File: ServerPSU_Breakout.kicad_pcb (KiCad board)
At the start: 2 copper layers, 120 x 90 mm, 25 parts, among them J1 Conn_01x05, J2 Conn_01x14, J3 Conn_01x01, J4 Conn_01x01, Q1 DMG2302U, U1 NCS1S1203SC, U2 STM32F072RBTx

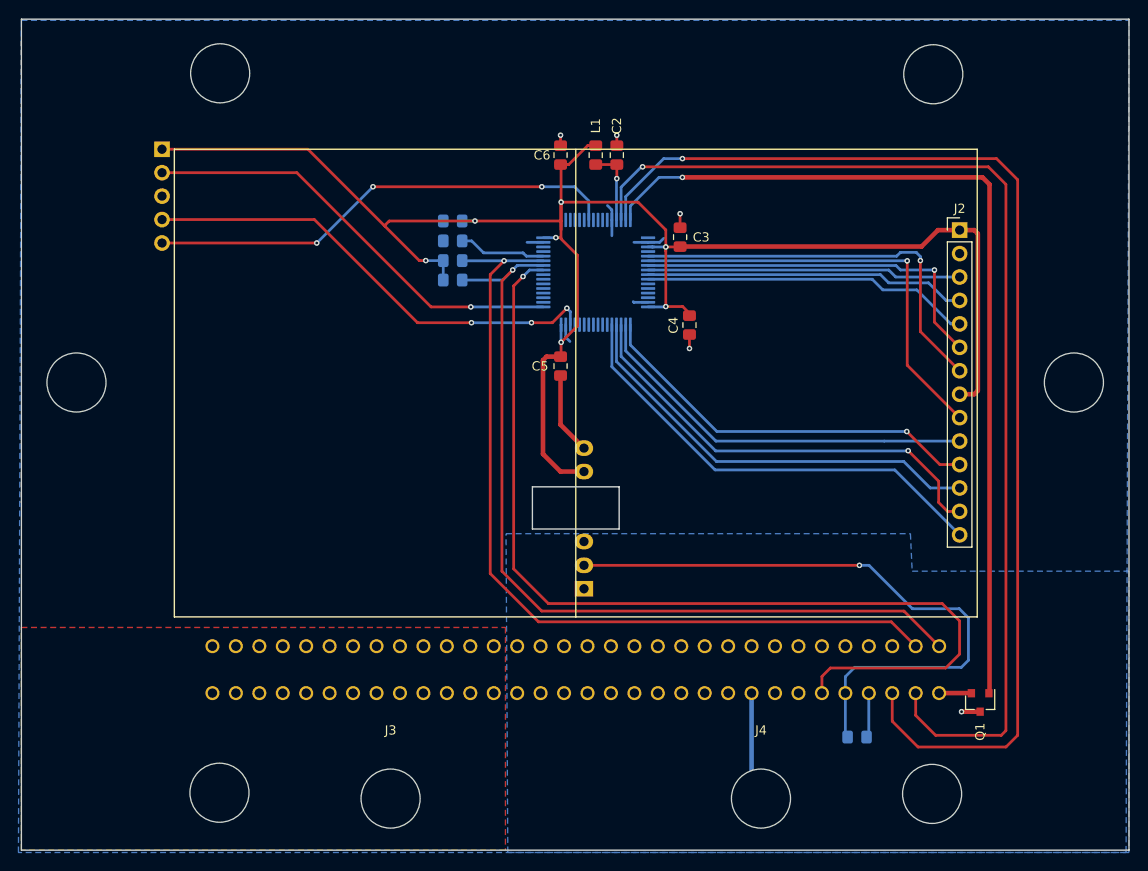
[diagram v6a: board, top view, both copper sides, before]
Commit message: updated hw
- added SMBUS address HW 
- Changed Isolated DC Module to TI SimpleSwitcher IC
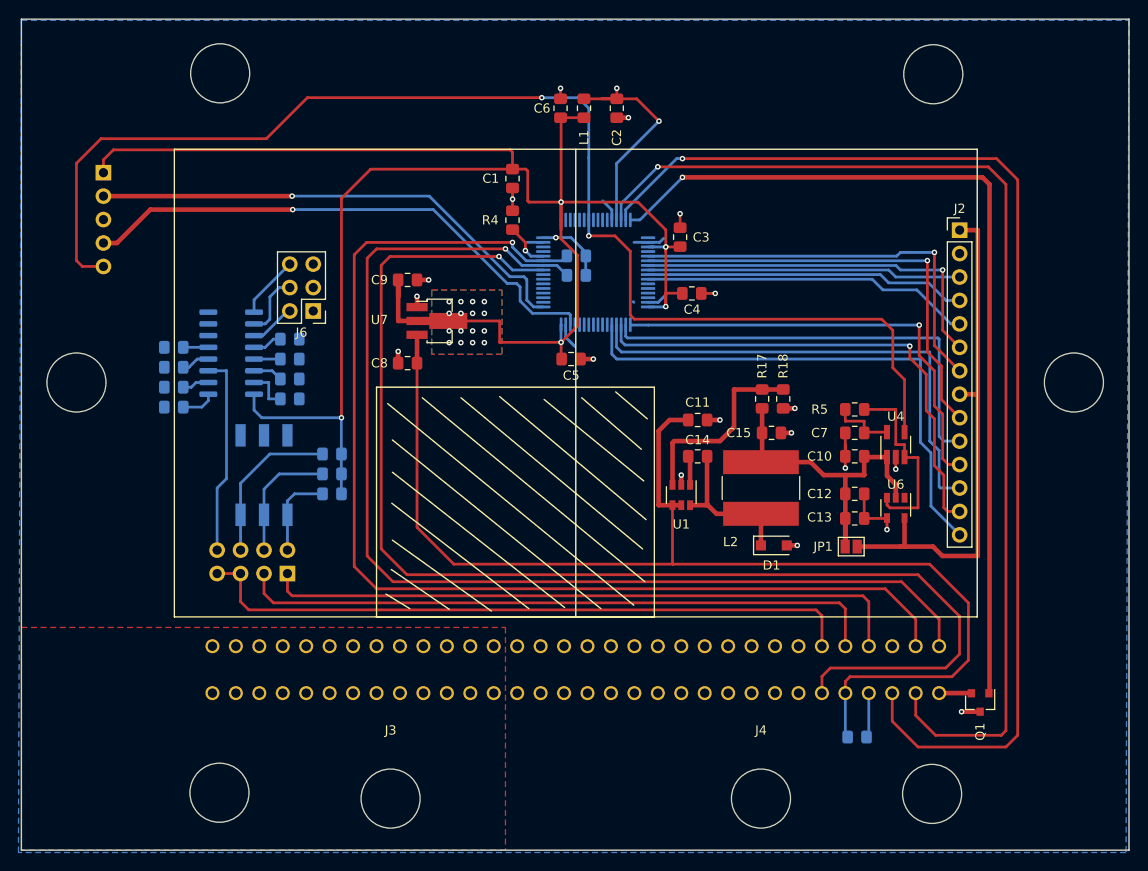
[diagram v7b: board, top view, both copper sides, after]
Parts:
- added C10: 100nF, Capacitor_SMD:C_0805_2012Metric_Pad1.15x1.40mm_HandSolder, F.Cu at (191.9, 94.2)
- added C11: 4.7uF X5R 25V, Capacitor_SMD:C_0805_2012Metric_Pad1.15x1.40mm_HandSolder, F.Cu at (174.9, 90.3)
- added C12: 1uF Low ESR, Capacitor_SMD:C_0805_2012Metric_Pad1.15x1.40mm_HandSolder, F.Cu at (191.9, 98.3)
- added C13: 100nF Low ESR, Capacitor_SMD:C_0805_2012Metric_Pad1.15x1.40mm_HandSolder, F.Cu at (191.9, 101.0)
- added C14: 200nF, Capacitor_SMD:C_0805_2012Metric_Pad1.15x1.40mm_HandSolder, F.Cu at (174.9, 94.2)
- added C15: 33uF X5R 10V, Capacitor_SMD:C_0805_2012Metric_Pad1.15x1.40mm_HandSolder, F.Cu at (182.9, 91.7)
- added C7: 2.2uF, Capacitor_SMD:C_0805_2012Metric_Pad1.15x1.40mm_HandSolder, F.Cu at (191.9, 91.7)
- added C8: 100nF, Capacitor_SMD:C_0805_2012Metric_Pad1.15x1.40mm_HandSolder, F.Cu at (143.4, 84.1)
- added C9: 100nF, Capacitor_SMD:C_0805_2012Metric_Pad1.15x1.40mm_HandSolder, F.Cu at (143.4, 75.1)
- added D1: SS14L, Diode_SMD:D_SOD-123F, F.Cu at (183.1, 103.9)
- added J5: Conn_02x04_Odd_Even, Connector_PinHeader_2.54mm:PinHeader_2x04_P2.54mm_Vertical, B.Cu at (130.4, 106.9)
- added J6: Conn_02x03_Odd_Even, Connector_PinHeader_2.54mm:PinHeader_2x03_P2.54mm_Vertical, F.Cu at (133.2, 78.5)
- added JP1: Jumper_NO_Small, Jumper:SolderJumper-2_P1.3mm_Open_Pad1.0x1.5mm, F.Cu at (191.5, 104.0)
- added L2: 18uH 150mOhm, Inductor_SMD:L_Bourns-SRN8040_8x8.15mm, F.Cu at (181.7, 97.7)
- added R10: 2K2, Resistor_SMD:R_0805_2012Metric_Pad1.15x1.40mm_HandSolder, B.Cu at (130.7, 85.9)
- added R11: 4K6, Resistor_SMD:R_0805_2012Metric_Pad1.15x1.40mm_HandSolder, B.Cu at (130.7, 88.0)
- added R12: 7K5, Resistor_SMD:R_0805_2012Metric_Pad1.15x1.40mm_HandSolder, B.Cu at (130.7, 81.5)
- added R13: 12K7, Resistor_SMD:R_0805_2012Metric_Pad1.15x1.40mm_HandSolder, B.Cu at (118.1, 88.9)
- added R14: 21K5, Resistor_SMD:R_0805_2012Metric_Pad1.15x1.40mm_HandSolder, B.Cu at (118.1, 82.4)
- added R15: 48K7, Resistor_SMD:R_0805_2012Metric_Pad1.15x1.40mm_HandSolder, B.Cu at (118.1, 86.7)
- added R16: 100K, Resistor_SMD:R_0805_2012Metric_Pad1.15x1.40mm_HandSolder, B.Cu at (118.1, 84.6)
- added R17: 5.6K, Resistor_SMD:R_0805_2012Metric_Pad1.15x1.40mm_HandSolder, F.Cu at (181.9, 88.0)
- added R18: 1K, Resistor_SMD:R_0805_2012Metric_Pad1.15x1.40mm_HandSolder, F.Cu at (184.2, 88.0)
- added R5: 1Meg, Resistor_SMD:R_0805_2012Metric_Pad1.15x1.40mm_HandSolder, F.Cu at (191.9, 89.2)
- added R6: 4K7, Resistor_SMD:R_0805_2012Metric_Pad1.15x1.40mm_HandSolder, B.Cu at (135.3, 98.3)
- added R7: 4K7, Resistor_SMD:R_0805_2012Metric_Pad1.15x1.40mm_HandSolder, B.Cu at (135.3, 96.1)
- added R8: 4K7, Resistor_SMD:R_0805_2012Metric_Pad1.15x1.40mm_HandSolder, B.Cu at (135.3, 94.0)
- added R9: 0R, Resistor_SMD:R_0805_2012Metric_Pad1.15x1.40mm_HandSolder, B.Cu at (130.7, 83.7)
- added SW1: SW_DIP_x03, Button_Switch_SMD:SW_DIP_SPSTx03_Slide_6.7x9.18mm_W8.61mm_P2.54mm_LowProfile, B.Cu at (127.9, 96.3)
- added U3: 4051, Package_SO:SOIC-16_3.9x9.9mm_P1.27mm, B.Cu at (124.3, 83.1)
- added U4: MIC1555-YM5, Package_TO_SOT_SMD:SOT-23-5_HandSoldering, F.Cu at (196.3, 93.0)
- added U6: MCP1415, Package_TO_SOT_SMD:SOT-23-5, F.Cu at (196.3, 99.8)
- added U7: AZ1117-3.3, Package_TO_SOT_SMD:SOT-89-3_Handsoldering, F.Cu at (146.6, 79.6)
- C1, R4: moved to F.Cu
- J1: footprint Connector_PinHeader_2.54mm:PinHeader_1x05_P2.54mm_Vertical -> Connector_PinHeader_2.54mm:PinHeader_1x05_P2.54mm_Horizontal
- U1: value NCS1S1203SC -> LMR14206; footprint Converter_DCDC:Converter_DCDC_Murata_NCS1SxxxxSC_THT -> Package_TO_SOT_SMD:SOT-23-6; moved to F.Cu
- moved U1 14.6 mm to (173.1, 98.4), turned to 270 degrees
- moved R1 13.4 mm to (161.7, 74.6), turned to 180 degrees
- moved R2 13.4 mm to (161.7, 72.5), turned to 180 degrees
- moved C1 7.94 mm to (154.8, 64.1), turned to 270 degrees
- moved R4 6.86 mm to (154.8, 68.6), turned to 90 degrees
- moved J1 6.84 mm to (110.5, 63.5)
- moved L1 5.24 mm to (162.6, 56.5), turned to 90 degrees
- moved C2 5.08 mm to (166.1, 56.5), turned to 90 degrees
- moved C6 5.08 mm to (160.0, 56.5)
- moved C4 3.44 mm to (174.2, 76.6), turned to 180 degrees
- moved C5 1.37 mm to (161.2, 83.7), turned to 180 degrees
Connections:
- net /HighVoltageControl/MCU_SW renamed /HighVoltageControl/MCU_SW_IN
- net /MCU/T_CLK renamed /MCU/TS_SCK
- net /MCU/T_CS renamed /MCU/TS_CS
- net /MCU/T_DIN renamed /MCU/TS_MOSI
- net /MCU/T_IRQ renamed /MCU/TS_IRQ
- net /MCU/T_OUT renamed /MCU/TS_MISO
- C1 pad 2: /HighVoltageControl/MCU_GND -> GNDS
- C2 pad 1: /HighVoltageControl/MCU_GND -> GNDS
- C3 pad 1: /HighVoltageControl/MCU_GND -> GNDS
- C4 pad 1: /HighVoltageControl/MCU_GND -> GNDS
- C5 pad 1: /HighVoltageControl/MCU_GND -> GNDS
- C6 pad 1: /HighVoltageControl/MCU_GND -> GNDS
- J1 pad 3: /HighVoltageControl/MCU_GND -> GNDS
- J2 pad 1: /HighVoltageControl/MCU_3V3 -> /MCU/TFT_DelayedReset/TFT_VDD_OUT
- J2 pad 2: /HighVoltageControl/MCU_GND -> GNDS
- J2 pad 8: /HighVoltageControl/MCU_3V3 -> /MCU/TFT_DelayedReset/TFT_VDD_OUT
- R4 pad 2: /HighVoltageControl/MCU_GND -> GNDS
- U1 pad 1: GNDS -> Net-(C14-Pad2)
- U1 pad 2: /HighVoltageControl/PSU_12VSB -> GNDS
- U1 pad 6: /HighVoltageControl/MCU_3V3 -> Net-(C14-Pad1)
- U2 pad 12: /HighVoltageControl/MCU_GND -> GNDS
- U2 pad 18: /HighVoltageControl/MCU_GND -> GNDS
- U2 pad 2: /PSUConnector/PSU_ADDR0 -> Net-(U2-Pad2)
- U2 pad 3: /PSUConnector/PSU_ADDR1 -> Net-(U2-Pad3)
- U2 pad 31: /HighVoltageControl/MCU_GND -> GNDS
- U2 pad 4: /PSUConnector/PSU_ADDR2 -> Net-(U2-Pad4)
- U2 pad 47: /HighVoltageControl/MCU_GND -> GNDS
- U2 pad 63: /HighVoltageControl/MCU_GND -> GNDS
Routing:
- net /MCU/NRST: track 51.5 -> 139.3 mm, vias 3 -> 2
- net /PSUConnector/PSU_ADDR2: track 0.00 -> 73.3 mm
- net /PSUConnector/PSU_ADDR0: track 0.00 -> 70.2 mm
- net /PSUConnector/PSU_ADDR1: track 0.00 -> 69.9 mm
- net /HighVoltageControl/PSU_12VSB: track 69.4 -> 131.4 mm, vias 1 -> 0
- net /MCU/TFT_DelayedReset/TFT_VDD_OUT: track 0.00 -> 55.8 mm
- net /MCU/TFTRST_5V: track 0.00 -> 37.7 mm
- net GNDS: track 13.9 -> 47.0 mm, vias 1 -> 18
- net /PSUConnector/PSU_SDA: track 92.7 -> 124.8 mm
- net /PSUConnector/PSU_INT: track 106.6 -> 136.8 mm
- net /PSUConnector/PSU_SCL: track 93.3 -> 123.2 mm
- net /HighVoltageControl/MCU_3V3: track 193.4 -> 221.3 mm, vias 7 -> 22
- net /HighVoltageControl/MCU_GND: track 26.5 -> 0.00 mm, vias 4 -> 0
- net Net-(J5-Pad8): track 0.00 -> 21.8 mm
- net Net-(R17-Pad1): track 0.00 -> 21.4 mm
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- added copper zone on B.Cu, net /HighVoltageControl/MCU_3V3
- added copper zone on F.Cu, net /HighVoltageControl/MCU_3V3
- removed copper zone on B.Cu, net /HighVoltageControl/MCU_GND
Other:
- outline, holes or cut-outs redrawn

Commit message: Completed RevA
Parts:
- added REF**: MountingHole_3.2mm_M3, MountingHole:MountingHole_3.2mm_M3, F.Cu at (121.2, 64.9)
- added REF**: MountingHole_3.2mm_M3, MountingHole:MountingHole_3.2mm_M3, F.Cu at (121.2, 108.3)
- added TP1: TestPoint, TestPoint:TestPoint_Pad_1.0x1.0mm, F.Cu at (109.2, 63.5)
- added TP10: TestPoint, TestPoint:TestPoint_Pad_1.0x1.0mm, F.Cu at (133.6, 48.9)
- added TP11: TestPoint, TestPoint:TestPoint_Pad_1.0x1.0mm, F.Cu at (188.3, 112.6)
- added TP12: TestPoint, TestPoint:TestPoint_Pad_1.0x1.0mm, F.Cu at (190.9, 112.6)
- added TP13: TestPoint, TestPoint:TestPoint_Pad_1.0x1.0mm, F.Cu at (193.4, 112.6)
- added TP14: TestPoint, TestPoint:TestPoint_Pad_1.0x1.0mm, F.Cu at (198.5, 112.6)
- added TP15: TestPoint, TestPoint:TestPoint_Pad_1.0x1.0mm, F.Cu at (201.0, 112.6)
- added TP16: TestPoint, TestPoint:TestPoint_Pad_1.0x1.0mm, F.Cu at (196.0, 112.6)
- added TP17: TestPoint, TestPoint:TestPoint_Pad_1.0x1.0mm, F.Cu at (188.3, 122.0)
- added TP18: TestPoint, TestPoint:TestPoint_Pad_1.0x1.0mm, F.Cu at (201.0, 122.0)
- added TP19: TestPoint, TestPoint:TestPoint_Pad_1.0x1.0mm, F.Cu at (198.5, 122.0)
- added TP2: TestPoint, TestPoint:TestPoint_Pad_1.0x1.0mm, F.Cu at (109.2, 68.6)
- added TP20: TestPoint, TestPoint:TestPoint_Pad_1.0x1.0mm, F.Cu at (196.0, 122.0)
- added TP21: TestPoint, TestPoint:TestPoint_Pad_1.0x1.0mm, F.Cu at (193.4, 122.0)
- added TP22: TestPoint, TestPoint:TestPoint_Pad_1.0x1.0mm, F.Cu at (109.2, 66.0)
- added TP23: TestPoint, TestPoint:TestPoint_Pad_1.0x1.0mm, F.Cu at (109.2, 71.1)
- added TP3: TestPoint, TestPoint:TestPoint_Pad_1.0x1.0mm, F.Cu at (185.8, 122.0)
- added TP4: TestPoint, TestPoint:TestPoint_Pad_1.0x1.0mm, F.Cu at (190.9, 122.0)
- added TP5: TestPoint, TestPoint:TestPoint_Pad_1.0x1.0mm, F.Cu at (170.1, 52.6)
- added TP6: TestPoint, TestPoint:TestPoint_Pad_1.0x1.0mm, F.Cu at (170.1, 50.5)
- added TP7: TestPoint, TestPoint:TestPoint_Pad_1.0x1.0mm, F.Cu at (161.8, 56.8)
- added TP8: TestPoint, TestPoint:TestPoint_Pad_1.0x1.0mm, F.Cu at (161.8, 54.7)
- added TP9: TestPoint, TestPoint:TestPoint_Pad_1.0x1.0mm, F.Cu at (133.6, 50.9)
- J3, J4: footprint MountingHole:MountingHole_6.4mm_M6 -> MountingHole:MountingHole_4.3mm_M4_Pad_Via
- R1, R2, R3: moved to F.Cu
- moved U4 66.0 mm to (145.0, 51.4), turned to 180 degrees
- moved JP1 64.7 mm to (154.2, 51.2), turned to 270 degrees
- moved R5 63.8 mm to (137.4, 55.9), turned to 90 degrees
- moved U6 63.7 mm to (150.4, 55.8)
- moved C7 62.1 mm to (141.2, 55.9), turned to 90 degrees
- moved C13 60.0 mm to (157.9, 51.6), turned to 270 degrees
- moved C10 59.6 mm to (146.3, 55.9), turned to 270 degrees
- moved C12 55.6 mm to (161.8, 51.6), turned to 90 degrees
- moved D1 52.6 mm to (187.4, 51.4), turned to 90 degrees
- moved U1 45.7 mm to (190.5, 56.2), turned to 90 degrees
- moved L2 44.8 mm to (180.6, 52.8), turned to 180 degrees
- moved C11 42.0 mm to (191.5, 51.7), turned to 90 degrees
- moved C15 41.2 mm to (173.4, 51.6), turned to 270 degrees
- moved C14 40.0 mm to (187.3, 56.3), turned to 270 degrees
- moved R18 34.0 mm to (170.0, 57.1), turned to 270 degrees
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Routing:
- net /HighVoltageControl/PSU_12VSB: track 131.4 -> 222.0 mm
- net /MCU/NRST: track 139.3 -> 97.8 mm, vias 2 -> 1
- net /MCU/TFT_DelayedReset/TFT_VDD_OUT: track 55.8 -> 87.1 mm
- net /PSUConnector/PSU_ADDR2: track 73.3 -> 99.5 mm
- net /PSUConnector/PSU_ADDR1: track 69.9 -> 96.1 mm
- net /HighVoltageControl/MCU_3V3: track 221.3 -> 198.0 mm
- net /MCU/AVDD: track 24.5 -> 9.72 mm, vias 2 -> 1
- net GNDS: track 47.0 -> 61.8 mm, vias 18 -> 19
- net /PSUConnector/PSU_ADDR0: track 70.2 -> 84.5 mm
- net Net-(J5-Pad2): track 9.45 -> 21.3 mm
- net Net-(C14-Pad1): track 17.0 -> 8.66 mm
- net Net-(J5-Pad4): track 13.6 -> 22.0 mm
- net Net-(J5-Pad8): track 21.8 -> 16.8 mm
- net /MCU/TFTRST_5V: track 37.7 -> 42.5 mm
- net Net-(C7-Pad2): track 7.09 -> 10.3 mm
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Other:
- board text added: "12V 60A WARNING: HIGH CURRENT!"
- board text added: "12VSB"
- board text added: "3V3"
- board text added: "5V"
- board text added: "A"
- board text added: "A0"
- board text added: "A1"
- board text added: "A2"
- board text added: "B"
- board text added: "C"
- board text added: "GND"
- board text added: "HPE CommonSlot PSU Controller RevA 07/20"
- board text added: "HPE MODE"
- board text added: "IMON"
- board text added: "INT"
- board text added: "MURATA MODE"
- board text added: "NRST"
- board text added: "OK"
- board text added: "ON"
- board text added: "PRES"
- board text added: "SCK"
- board text added: "SCL"
- board text added: "SDA"
- board text added: "SWD"
- board text added: "TFT5V"
